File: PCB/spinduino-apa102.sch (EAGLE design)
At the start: 23 parts

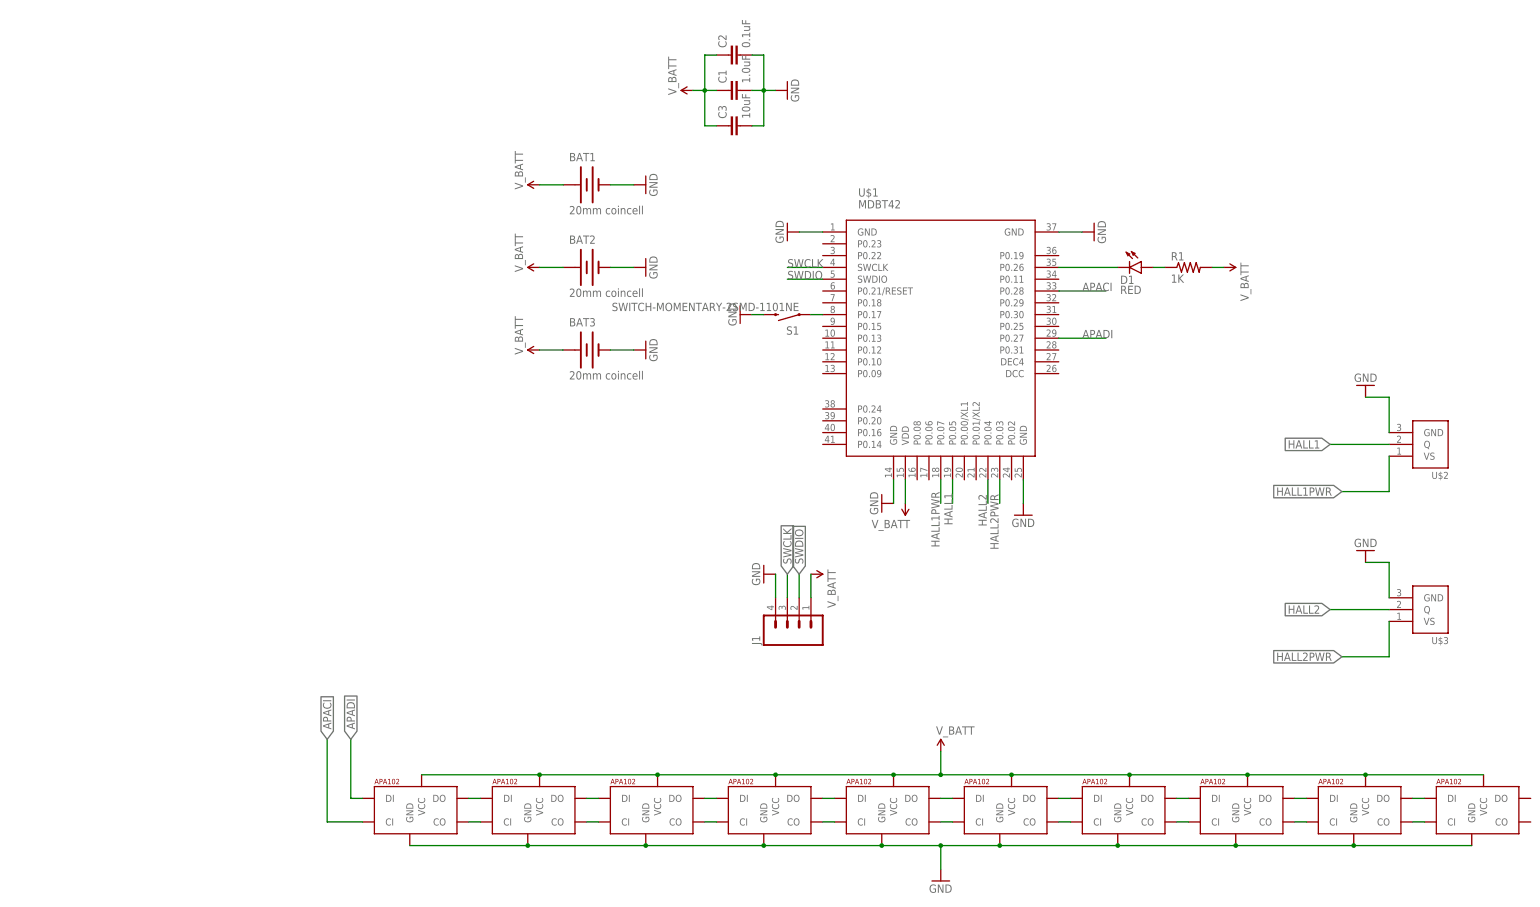
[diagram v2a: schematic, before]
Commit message: feat: powed the LEDs by 5V pump
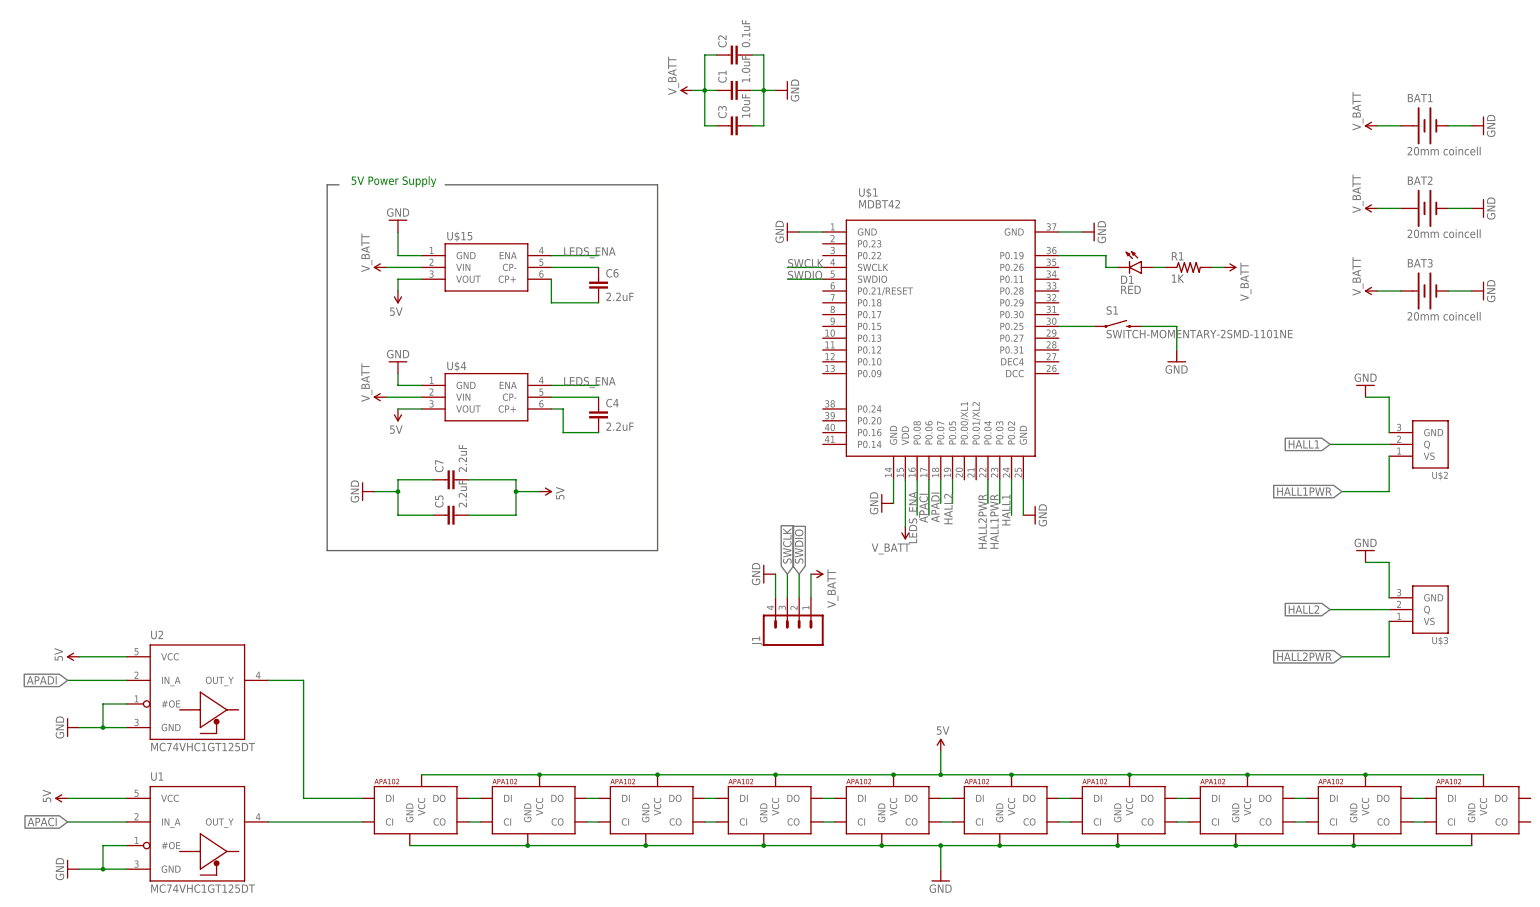
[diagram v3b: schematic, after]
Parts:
- added C4, C6: 2.2uF, SparkFun-Capacitors:2.2UF-10V-20%(0603)
- added C5, C7: 2.2uF, SparkFun-Capacitors:10UF-6.3V-20%(0603)
- added U$15, U$4: TPS60150, uri:TPS60150
- added U1, U2: MC74VHC1GT125DT, uri:MC74VHC1GT125DT
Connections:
- new net 5V: C5.2, C7.2, U$10.VCC, U$11.VCC, U$12.VCC, U$13.VCC, U$14.VCC, U$15.VOUT, U$4.VOUT, U$5.VCC, U$6.VCC, U$7.VCC, U$8.VCC, U$9.VCC, U1.VCC, U2.VCC
- new net LEDS_ENA: U$1.P0.08, U$15.ENA, U$4.ENA
- new net N$22: C4.2, U$4.CP+
- new net N$23: C4.1, U$4.CP-
- new net N$24: U$14.DI, U2.OUT_Y
- new net N$25: U$14.CI, U1.OUT_Y
- new net N$26: C6.1, U$15.CP-
- new net N$29: C6.2, U$15.CP+
- net APACI: now also U$1.P0.06, U1.IN_A; no longer U$1.P0.28, U$14.CI
- net APADI: now also U$1.P0.07, U2.IN_A; no longer U$1.P0.27, U$14.DI
- net GND: now also C5.1, C7.1, U$15.GND, U$4.GND, U1.#OE, U1.GND, U2.#OE, U2.GND
- net HALL1: now also U$1.P0.02; no longer U$1.P0.05
- net HALL1PWR: now also U$1.P0.03; no longer U$1.P0.07
- net HALL2: now also U$1.P0.05; no longer U$1.P0.04
- net HALL2PWR: now also U$1.P0.04; no longer U$1.P0.03
- net N$21: now also U$1.P0.25; no longer U$1.P0.17
- net N$3: now also U$1.P0.19; no longer U$1.P0.26
- net V_BATT: now also U$15.VIN, U$4.VIN; no longer U$10.VCC, U$11.VCC, U$12.VCC, U$13.VCC, U$14.VCC, U$5.VCC, U$6.VCC, U$7.VCC, U$8.VCC, U$9.VCC
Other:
- note added: "5V Power Supply"
- moved on the sheet: BAT1, BAT2, BAT3, S1

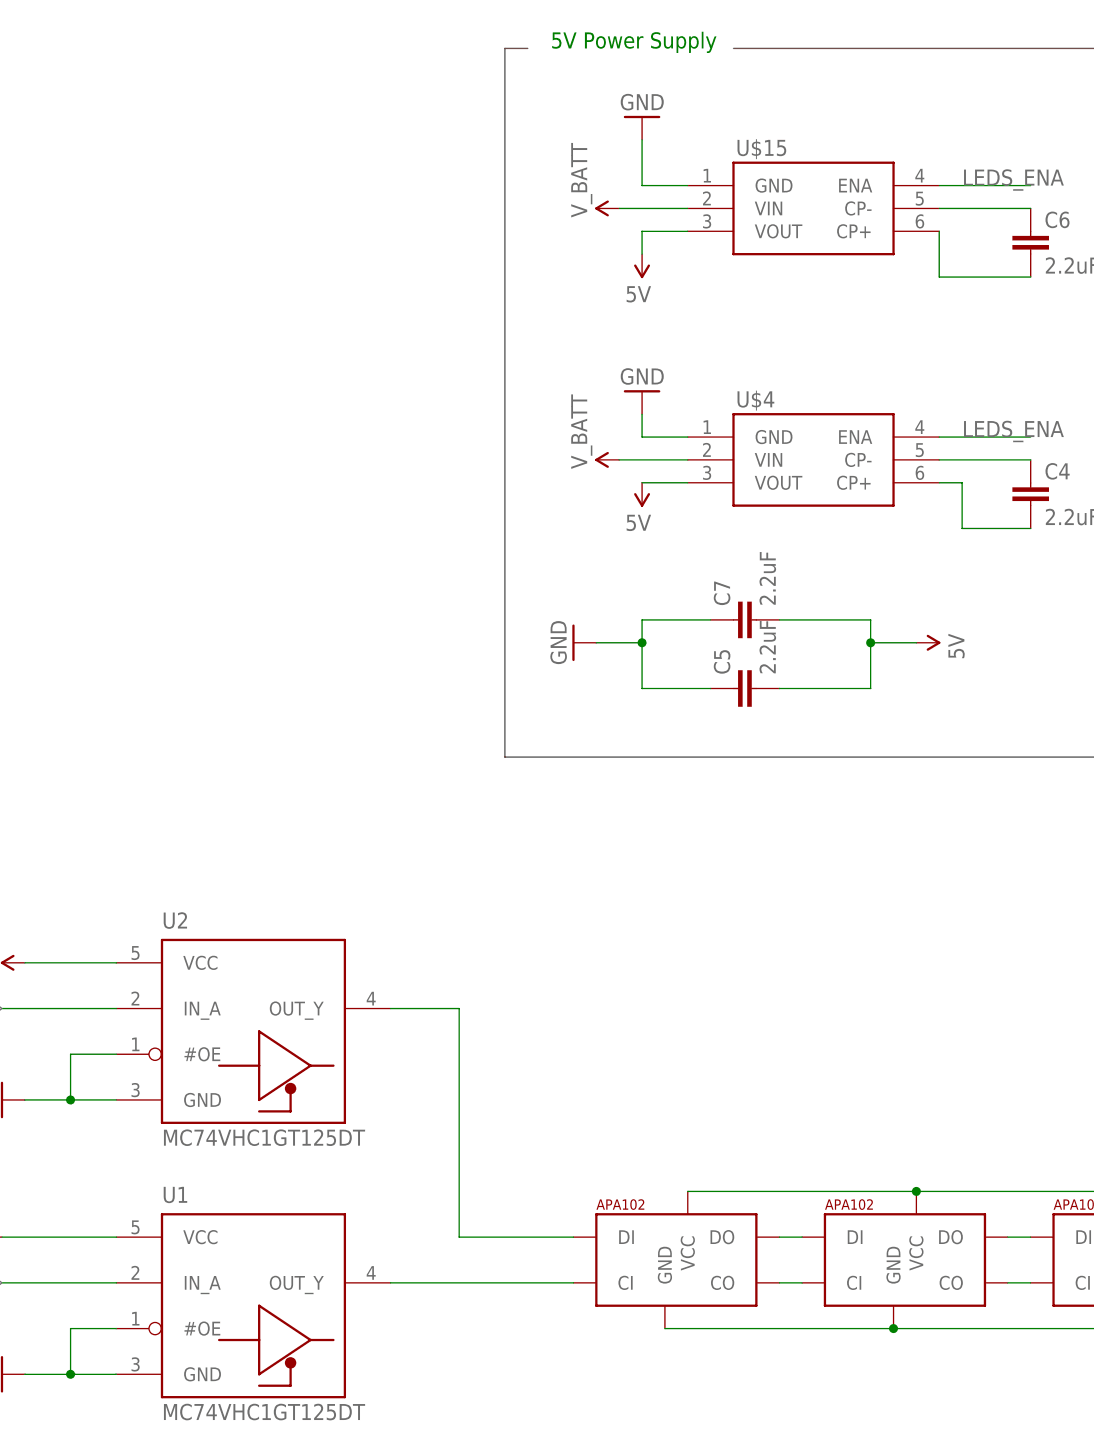
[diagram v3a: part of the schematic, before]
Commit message: fix a few issues in board:
1. remove copper under antenna
2. fix wrong pin assignments of TPS60150
3. shrink inner hole a bit
4. fix package for MC74VHC1GT125 (SOT353 instead of SOT23-5)
5. move text to a different wing
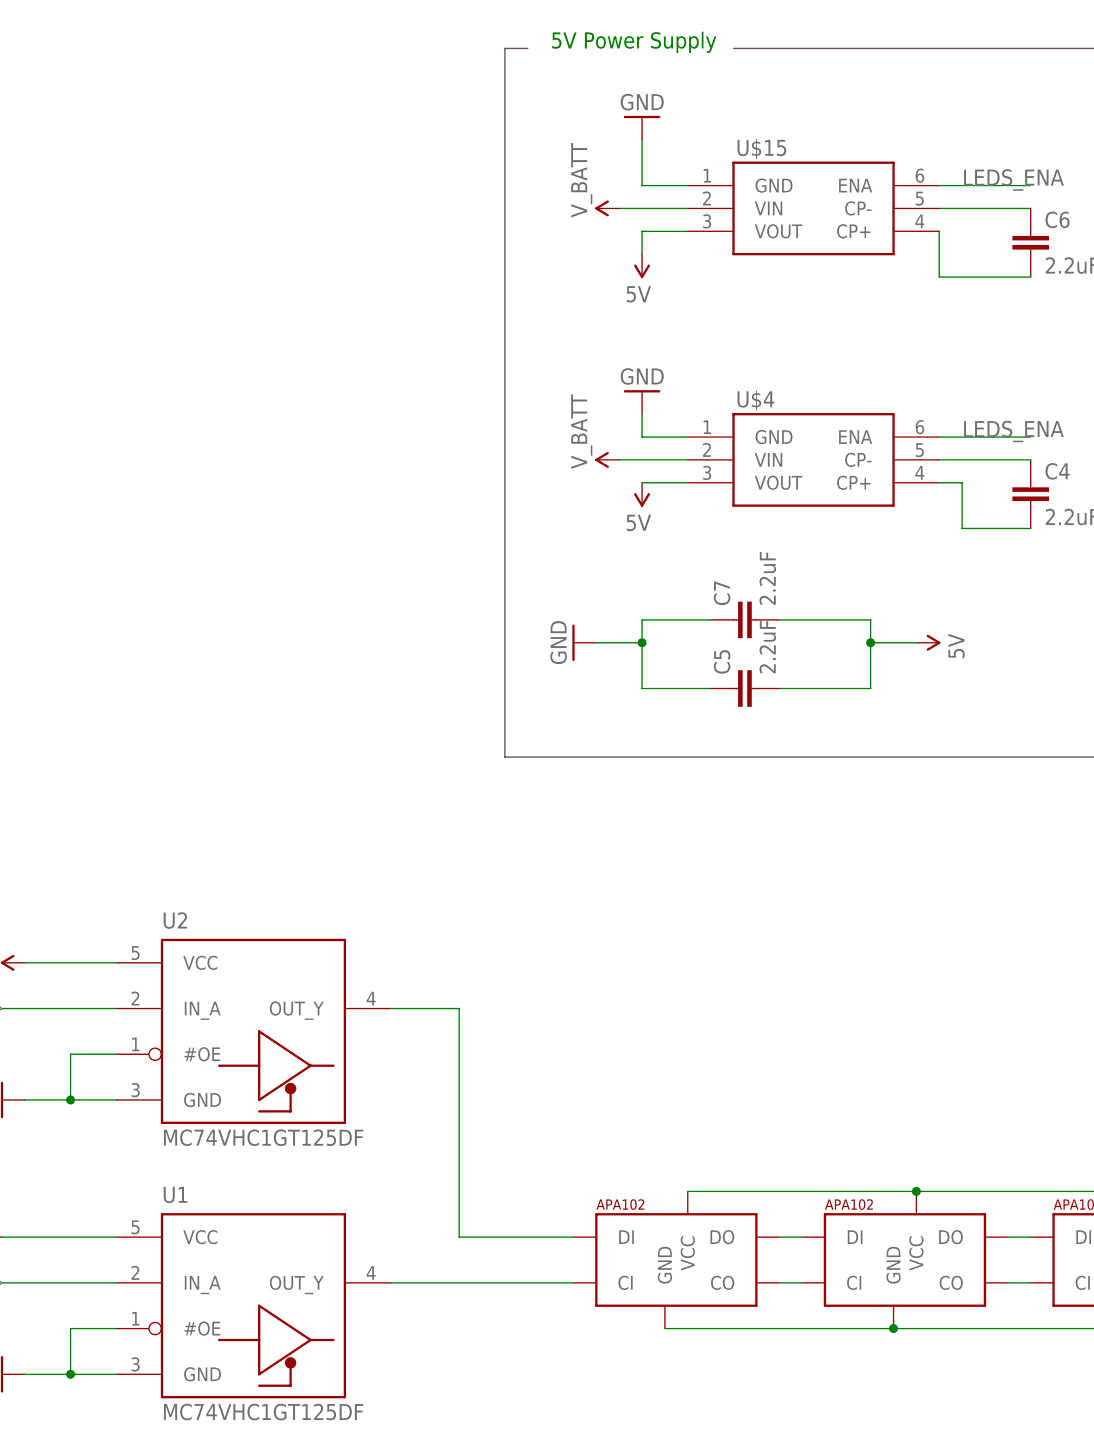
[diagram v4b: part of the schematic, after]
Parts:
- U1, U2: value MC74VHC1GT125DT -> MC74VHC1GT125DF; device uri:MC74VHC1GT125DT -> uri:MC74VHC1GT125DF
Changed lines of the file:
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@@
 <part name="SUPPLY6" library="SparkFun-Aesthetics" deviceset="5V" device=""/>
 <part name="SUPPLY9" library="SparkFun-Aesthetics" deviceset="V_BATT" device=""/>
-<part name="U1" library="uri" deviceset="MC74VHC1GT125" device="DT"/>
-<part name="U2" library="uri" deviceset="MC74VHC1GT125" device="DT"/>
+<part name="U1" library="uri" deviceset="MC74VHC1GT125" device="DF" value="MC74VHC1GT125DF"/>
+<part name="U2" library="uri" deviceset="MC74VHC1GT125" device="DF" value="MC74VHC1GT125DF"/>
 <part name="SUPPLY11" library="SparkFun-Aesthetics" deviceset="5V" device=""/>
 <part name="SUPPLY12" library="SparkFun-Aesthetics" deviceset="5V" device=""/>
